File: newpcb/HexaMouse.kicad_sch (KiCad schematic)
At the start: 12 parts, among them U1 XIAO-Add-On, U2 MLX90393SLW-ABA-011-RE, U3 MLX90393SLW-ABA-011-RE, U4 MLX90393SLW-ABA-011-RE

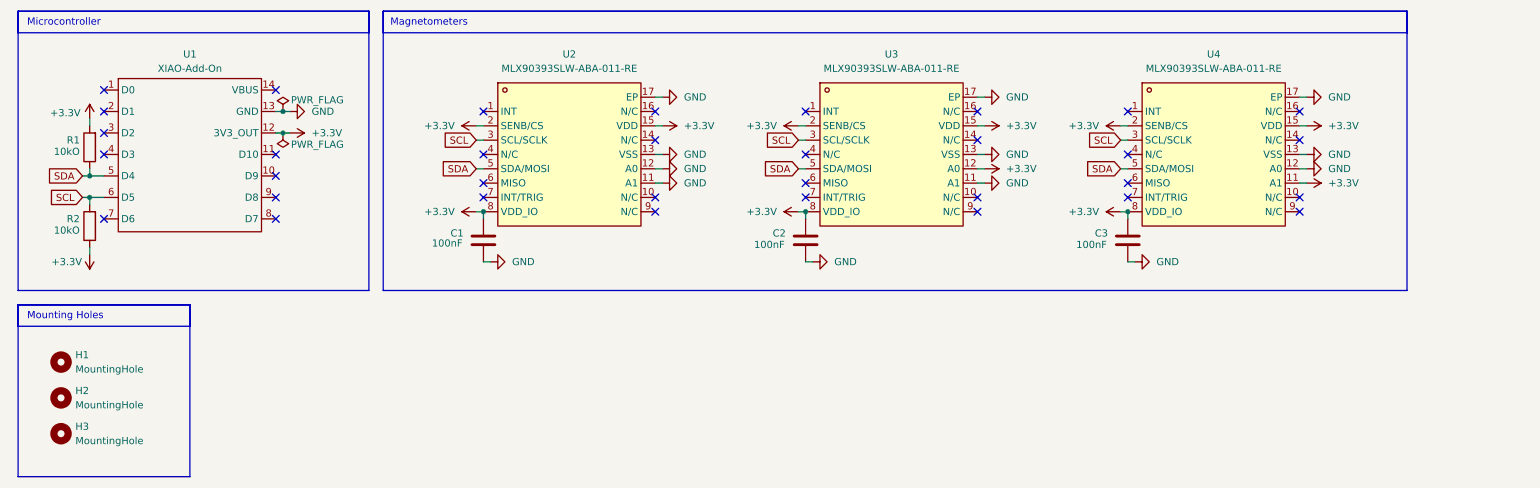
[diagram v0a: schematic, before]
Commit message: Added bulk decoupling cap
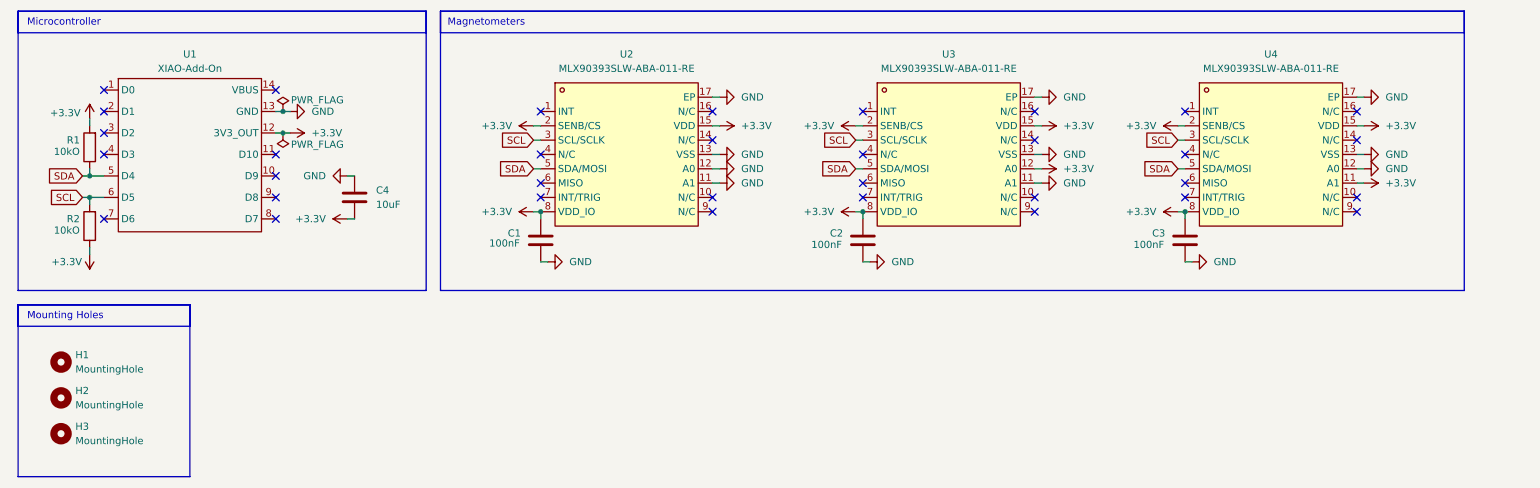
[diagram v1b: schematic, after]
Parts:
- added C4: 10uF, symbol Device:C
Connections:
- net +3.3V: now also C4.2
- net GND: now also C4.1
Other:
- moved on the sheet: C1, C2, C3, U2, U3, U4

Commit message: Added LEDs and Buttons to schematic
ERC all clear so can go to pcb now
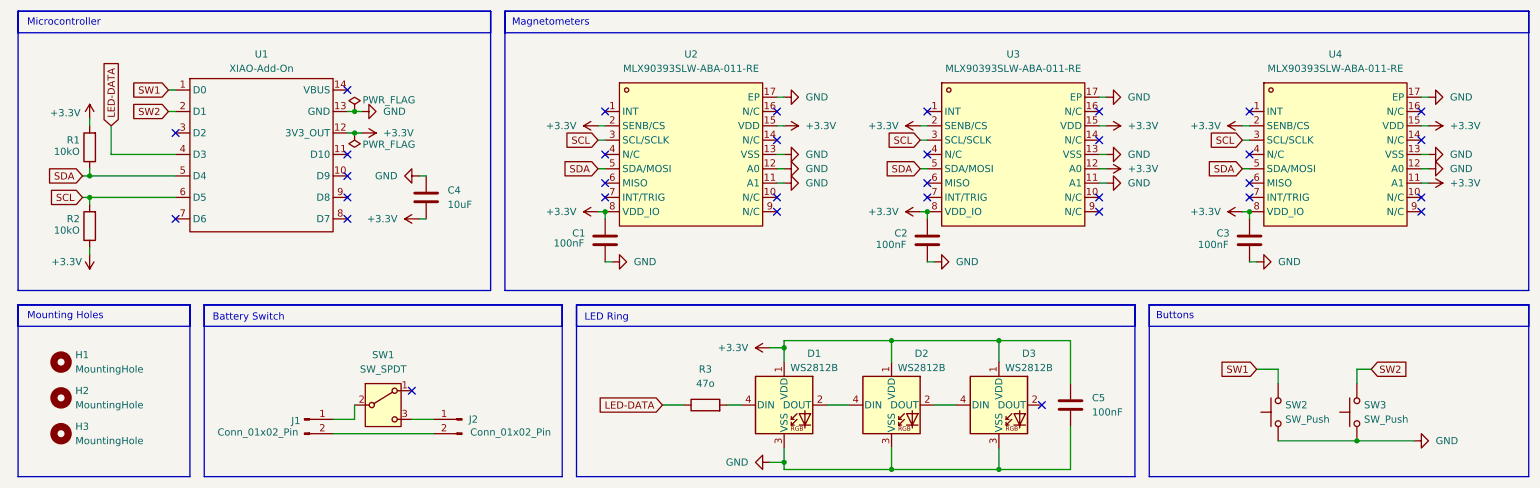
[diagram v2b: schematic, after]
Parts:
- added C5: 100nF, LED_SMD:LED_WS2812B_PLCC4_5.0x5.0mm_P3.2mm, symbol Device:C
- added D1, D2, D3: WS2812B, LED_SMD:LED_WS2812B_PLCC4_5.0x5.0mm_P3.2mm, symbol LED:WS2812B
- added J1, J2: Conn_01x02_Pin, symbol Connector:Conn_01x02_Pin
- added R3: 47o, symbol Device:R
- added SW1: SW_SPDT, Button_Switch_THT:SW_NKK_GW12LJP, symbol Switch:SW_SPDT
- added SW2, SW3: SW_Push, Button_Switch_THT:SW_NKK_GW12LJP, symbol Switch:SW_Push
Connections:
- net +3.3V: now also C5.1, D1.1 (VDD), D2.1 (VDD), D3.1 (VDD)
- net GND: now also C5.2, D1.3 (VSS), D2.3 (VSS), D3.3 (VSS), SW2.1, SW3.1
- net SW1: now reaches U1.1 (D0)
- net SW1: now also SW2.2
- net SW2: now reaches U1.2 (D1)
- net SW2: now also SW3.2
- net LED-DATA: now reaches U1.4 (D3)
- net LED-DATA: now also R3.1
- new net: J1.1 (Pin_1), SW1.2 (B)
- new net: J2.1 (Pin_1), SW1.3 (C)
- new net: J1.2 (Pin_2), J2.2 (Pin_2)
- new net: D2.2 (DOUT), D3.4 (DIN)
- new net: D1.2 (DOUT), D2.4 (DIN)
- new net: D1.4 (DIN), R3.2
- no-connect marks 34 -> 33
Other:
- note added: "Battery Switch"
- note added: "Buttons"
- note added: "LED Ring"
- moved on the sheet: C1, C2, C3, C4, U1, U2, U3, U4

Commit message: Did footprinting and lcsc
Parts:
- C1, C2, C3: footprint easyeda2kicad:VQFN-16_L3.0-W3.0-P0.50-BL-EP1.7 -> Capacitor_SMD:C_0603_1608Metric; LCSC (none) -> C14663
- C4: footprint (none) -> Capacitor_SMD:C_0603_1608Metric; LCSC (none) -> C96446
- C5: footprint LED_SMD:LED_WS2812B_PLCC4_5.0x5.0mm_P3.2mm -> Capacitor_SMD:C_0603_1608Metric; LCSC (none) -> C14663
- D1, D2, D3: LCSC (none) -> C2761795
- H1, H2, H3: footprint Package_DFN_QFN:WDFN-10-1EP_3x3mm_P0.5mm_EP1.8x2.5mm -> MountingHole:MountingHole_3.2mm_M3
- J1, J2: footprint (none) -> Connector_PinHeader_2.54mm:PinHeader_1x02_P2.54mm_Vertical
- R1, R2: footprint (none) -> Resistor_SMD:R_0603_1608Metric; LCSC (none) -> C25804
- R3: footprint (none) -> Resistor_SMD:R_0603_1608Metric; LCSC (none) -> C23182
- SW1: footprint Button_Switch_THT:SW_NKK_GW12LJP -> Button_Switch_SMD:SW_SPDT_PCM12; LCSC (none) -> C221841
- SW2, SW3: footprint Button_Switch_THT:SW_NKK_GW12LJP -> Button_Switch_SMD:SW_SPST_B3U-3000P-B; LCSC (none) -> C4364471
- U2, U3, U4: LCSC (none) -> C2649492

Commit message: Swapped battery nets
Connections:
- net at SW1.2 (B): now also J1.2 (Pin_2); no longer J1.1 (Pin_1)
- net at SW1.3 (C): now also J2.2 (Pin_2); no longer J2.1 (Pin_1)
- new net: J1.1 (Pin_1), J2.1 (Pin_1)
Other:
- moved on the sheet: J2
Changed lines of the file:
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@@
 	(wire
 		(pts
+			(xy 69.85 86.36) (xy 73.66 86.36)
+		)
+		(stroke
+			(width 0)
+			(type default)
+		)
+	)
+	(wire
+		(pts
 			(xy 262.89 29.21) (xy 264.16 29.21)
 		)
@@
 	(wire
 		(pts
-			(xy 83.82 86.36) (xy 87.63 86.36)
+			(xy 85.09 50.8) (xy 86.36 50.8)
 		)
 		(stroke
@@
 	(wire
 		(pts
-			(xy 85.09 50.8) (xy 86.36 50.8)
+			(xy 262.89 41.91) (xy 264.16 41.91)
 		)
 		(stroke
@@
 	(wire
 		(pts
-			(xy 262.89 41.91) (xy 264.16 41.91)
+			(xy 205.74 29.21) (xy 207.01 29.21)
 		)
 		(stroke
@@
 	(wire
 		(pts
-			(xy 205.74 29.21) (xy 207.01 29.21)
+			(xy 187.96 95.25) (xy 168.91 95.25)
 		)
 		(stroke
@@
 	(wire
 		(pts
-			(xy 187.96 95.25) (xy 168.91 95.25)
+			(xy 83.82 86.36) (xy 87.63 86.36)
 		)
 		(stroke
@@
 	(wire
 		(pts
-			(xy 73.66 86.36) (xy 69.85 86.36)
-		)
-		(stroke
-			(width 0)
-			(type default)
-		)
-	)
-	(wire
-		(pts
 			(xy 175.26 58.42) (xy 176.53 58.42)
 		)
@@
 	(symbol
 		(lib_id "Connector:Conn_01x02_Pin")
-		(at 64.77 86.36 0)
+		(at 64.77 88.9 0)
+		(mirror x)
 		(unit 1)
 		(body_style 1)
@@
 		(dnp no)
 		(property "Reference" "J1"
-			(at 63.246 86.614 0)
+			(at 63.246 88.646 0)
 			(show_name no)
 			(do_not_autoplace no)
@@
 		)
 		(property "Value" "Conn_01x02_Pin"
-			(at 56.515 88.646 0)
+			(at 56.515 86.614 0)
 			(show_name no)
 			(do_not_autoplace no)
@@
 		)
 		(property "Footprint" "Connector_PinHeader_2.54mm:PinHeader_1x02_P2.54mm_Vertical"
-			(at 64.77 86.36 0)
+			(at 64.77 88.9 0)
 			(hide yes)
 			(show_name no)
@@
 		)
 		(property "Datasheet" ""
-			(at 64.77 86.36 0)
+			(at 64.77 88.9 0)
 			(hide yes)
 			(show_name no)
@@
 		)
 		(property "Description" "Generic connector, single row, 01x02, script generated"
-			(at 64.77 86.36 0)
+			(at 64.77 88.9 0)
 			(hide yes)
 			(show_name no)
@@
 		)
 		(property "LCSC" ""
-			(at 64.77 86.36 0)
+			(at 64.77 88.9 0)
 			(hide yes)
 			(show_name no)
@@
 	(symbol
 		(lib_id "Connector:Conn_01x02_Pin")
-		(at 92.71 86.36 0)
-		(mirror y)
+		(at 92.71 88.9 180)
 		(unit 1)
 		(body_style 1)
@@
 		(dnp no)
 		(property "Reference" "J2"
-			(at 94.742 86.36 0)
+			(at 94.742 88.9 0)
 			(show_name no)
 			(do_not_autoplace no)
@@
 		)
 		(property "Value" "Conn_01x02_Pin"
-			(at 101.346 88.646 0)
+			(at 101.346 86.614 0)
 			(show_name no)
 			(do_not_autoplace no)
@@
 		)
 		(property "Footprint" "Connector_PinHeader_2.54mm:PinHeader_1x02_P2.54mm_Vertical"
-			(at 92.71 86.36 0)
+			(at 92.71 88.9 0)
 			(hide yes)
 			(show_name no)
@@
 		)
 		(property "Datasheet" ""
-			(at 92.71 86.36 0)
+			(at 92.71 88.9 0)
 			(hide yes)
 			(show_name no)
@@
 		)
 		(property "Description" "Generic connector, single row, 01x02, script generated"
-			(at 92.71 86.36 0)
+			(at 92.71 88.9 0)
 			(hide yes)
 			(show_name no)
@@
 		)
 		(property "LCSC" ""
-			(at 92.71 86.36 0)
+			(at 92.71 88.9 0)
 			(hide yes)
 			(show_name no)
